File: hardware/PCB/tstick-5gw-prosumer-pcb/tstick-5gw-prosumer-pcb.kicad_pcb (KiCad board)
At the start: 2 copper layers, 171.5 x 31.8 mm, 41 parts, among them Q1 BSS138, Q2 BSS138, SW1 JSTCONNECTOR, U1 PCA9306DP

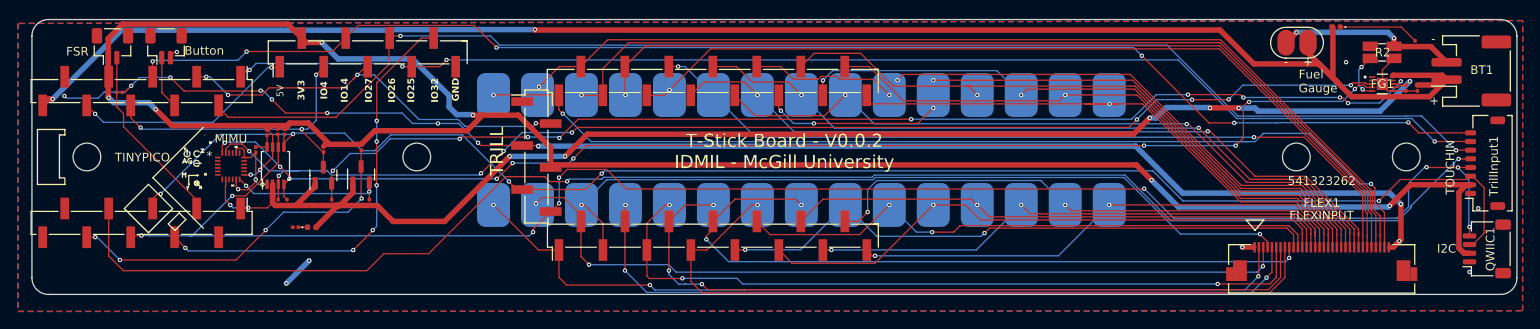
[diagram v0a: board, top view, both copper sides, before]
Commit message: updated kicad schematic for prsoumer t-stick board board
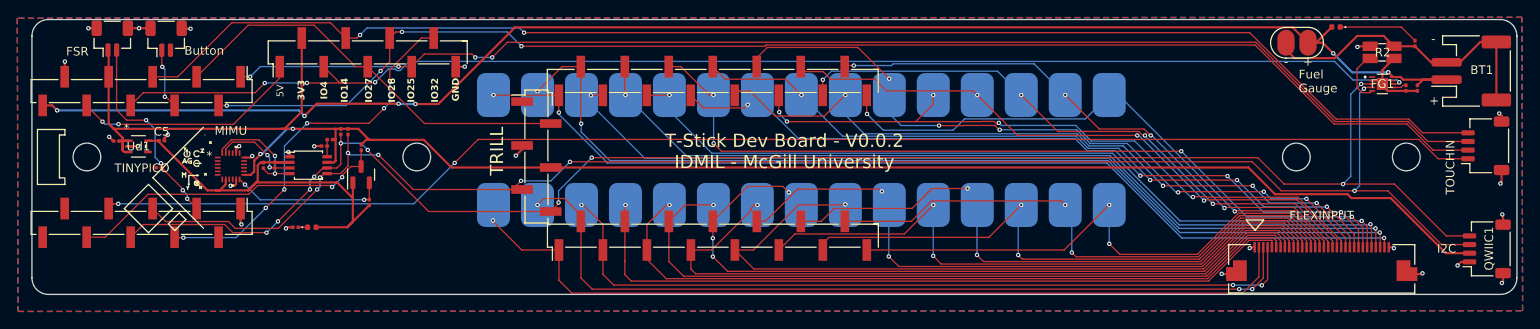
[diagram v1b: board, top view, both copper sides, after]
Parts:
- removed Q1: BSS138, Package_TO_SOT_SMD:SOT-23
- removed R3, R4: 10k, Resistor_SMD:R_0201_0603Metric
- added C4: 1uF, Capacitor_SMD:C_0201_0603Metric, F.Cu at (37.4, 84.4)
- added C5: 1uF, Capacitor_SMD:C_0201_0603Metric, F.Cu at (42.6, 84.4)
- added Ud1: MAX8511EXK18+T, max8511-footprints:21-0076_X5&plus_1_MXM, F.Cu at (39.9, 85.0)
- TrillInput1: footprint Connector_JST:JST_SHL_SM08B-SHLS-TF_1x08-1MP_P1.00mm_Horizontal -> Connector_JST:JST_SH_SM04B-SRSS-TB_1x04-1MP_P1.00mm_Horizontal
- moved R1 9.81 mm to (42.3, 87.5), turned to 180 degrees
- moved C3 7.93 mm to (61.4, 85.0), turned to 180 degrees
- moved R13 7.33 mm to (64.1, 83.4)
- moved R6 7.33 mm to (62.0, 84.3), turned to 0 degrees
- moved R7 7.29 mm to (63.3, 83.3)
- moved R5 5.07 mm to (54.4, 87.2), turned to 90 degrees
- moved R8 4.33 mm to (55.7, 87.2), turned to 90 degrees
- moved U1 3.81 mm to (59.5, 87.2), turned to 0 degrees
- moved TrillInput1 2.01 mm to (195.5, 85.0)
- moved FSR1 0.88 mm to (36.9, 72.6)
- moved SW1 0.87 mm to (43.1, 72.6)
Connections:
- BT1 pad MP: (no net) -> -BATT
- C2 pad 1: +1V8 -> /REG
- FG1 pad 3: /LV_SCL -> /SCL
- FG1 pad 4: /LV_SDA -> /SDA
- FG1 pad 7: +1V8 -> /REG
- FG1 pad 8: /FG_INT -> /IO4
- FSR1 pad MP: (no net) -> GND
- QWIIC1 pad MP: (no net) -> GND
- SW1 pad MP: (no net) -> GND
- TrillInput1 pad 1: GND -> /IO5/SS
- TrillInput1 pad 2: +3V3 -> /IO26
- TrillInput1 pad 3: /SDA -> /IO25
- TrillInput1 pad 4: /SCL -> /IO14
- TrillInput1 pad MP: (no net) -> GND
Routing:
- net GND: track 187.4 -> 32.7 mm, vias 21 -> 26
- net /LV_SCL: track 144.4 -> 10.1 mm, vias 9 -> 2
- net /FG_INT: track 133.0 -> 0.00 mm, vias 10 -> 0
- net /LV_SDA: track 145.3 -> 13.2 mm, vias 10 -> 2
- net /IO4: track 34.6 -> 154.0 mm, vias 3 -> 4
- net +1V8: track 163.7 -> 50.8 mm, vias 8 -> 0
- net +3V3: track 244.3 -> 205.9 mm, vias 8 -> 2
- net -BATT: track 21.0 -> 36.9 mm, vias 2 -> 0
- net +BATT: track 191.2 -> 176.6 mm, vias 2 -> 6
- net /TOUCH08: track 70.4 -> 83.7 mm, vias 2 -> 1
- net /IO5/SS: track 173.8 -> 161.3 mm
- net /TOUCH27: track 109.2 -> 101.2 mm, vias 1 -> 2
- net /TOUCH12: track 61.8 -> 69.3 mm
- net /IO32: track 50.5 -> 44.7 mm
- net /TOUCH11: track 63.0 -> 68.7 mm, vias 1 -> 2
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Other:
- board text added: "T-Stick Dev Board - V0.0.2 IDMIL - McGill University"
- board text removed: "Center X = 27.6098 Y = 86.2716"
- board text removed: "T-Stick Board - V0.0.2 IDMIL - McGill University"
